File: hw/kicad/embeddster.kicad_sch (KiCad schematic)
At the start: 1 part, among them U1 ESP32-DEVKIT-V1

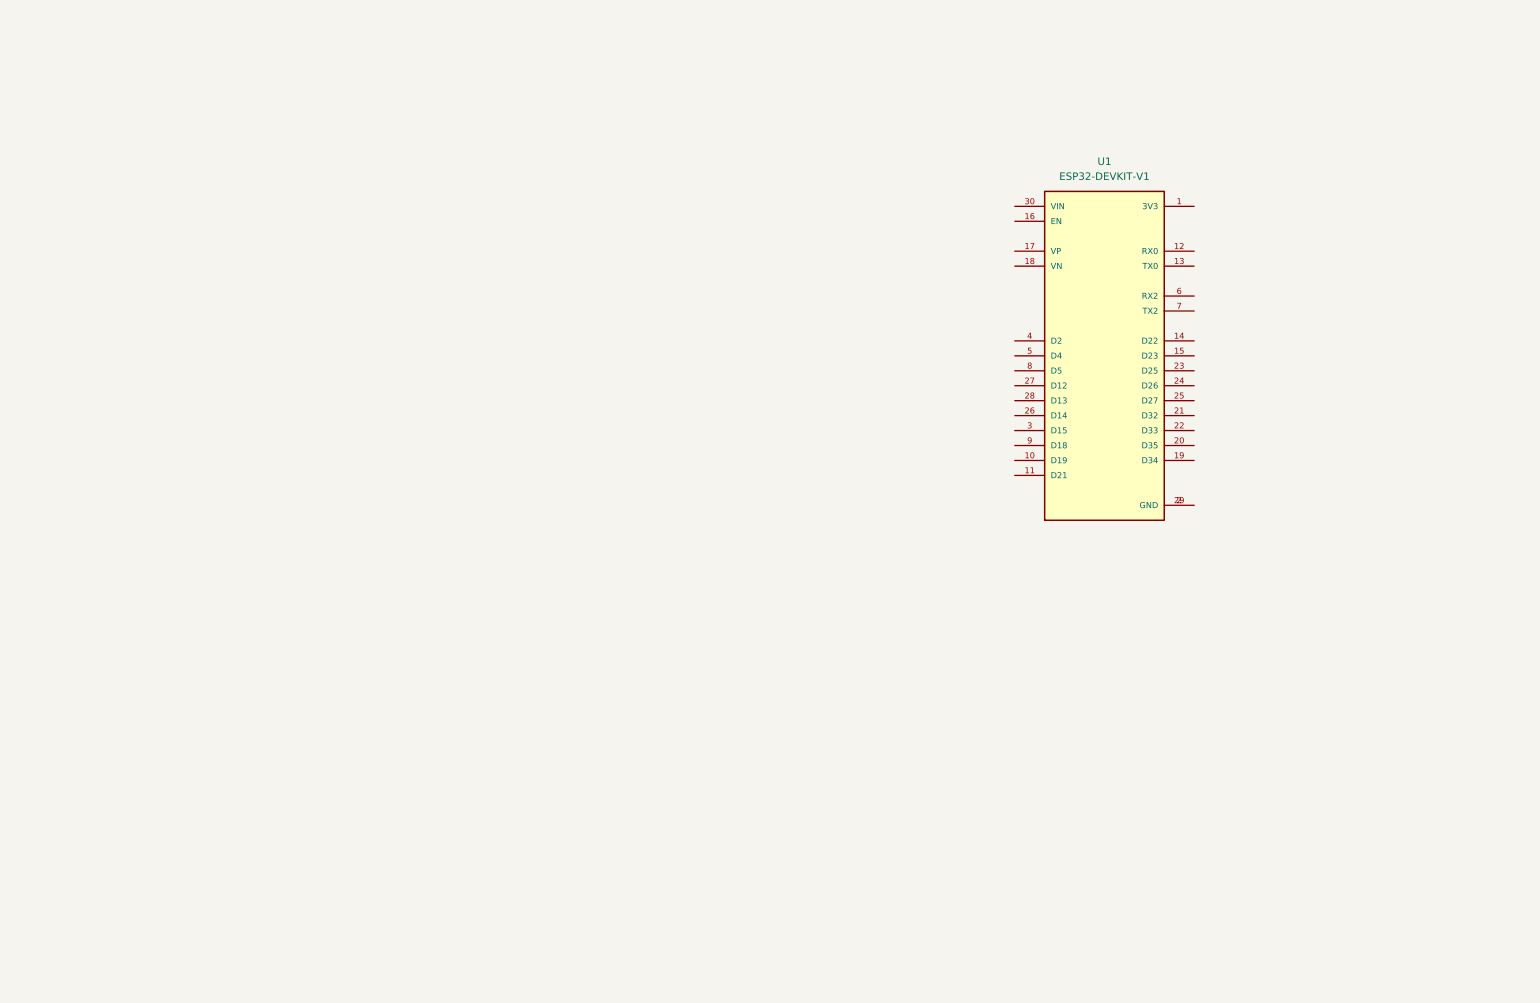
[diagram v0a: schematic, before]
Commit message: Pcb v0 (#1)
* Add custom KiCad symbol&footproint for PLACA_CAN_V20190517

* Add 3D models for PLACA_CAN_V20190517 connector pins

* Remove mounting holes from ESP32 footprint

* sch supporting tp1 & tp2

* Remove unnecessary zone definitions from ESP32 DevKit V1 footprint

* Add 3D models for ESP32 DevKit V1 connector pins

* pcb ready for fab

* Add pin assignment header for MCP, encoder, and 74HC595 control, based on PCB

* Add 4th quantum standoff to PCB, ground plane adjustments

* Add a WS2812B cell

* Add active low definition for encoder switch

* Update README to remove TP3 reference and clarify hardware interface

* Fix routing, remove old pic

* re-fix routing
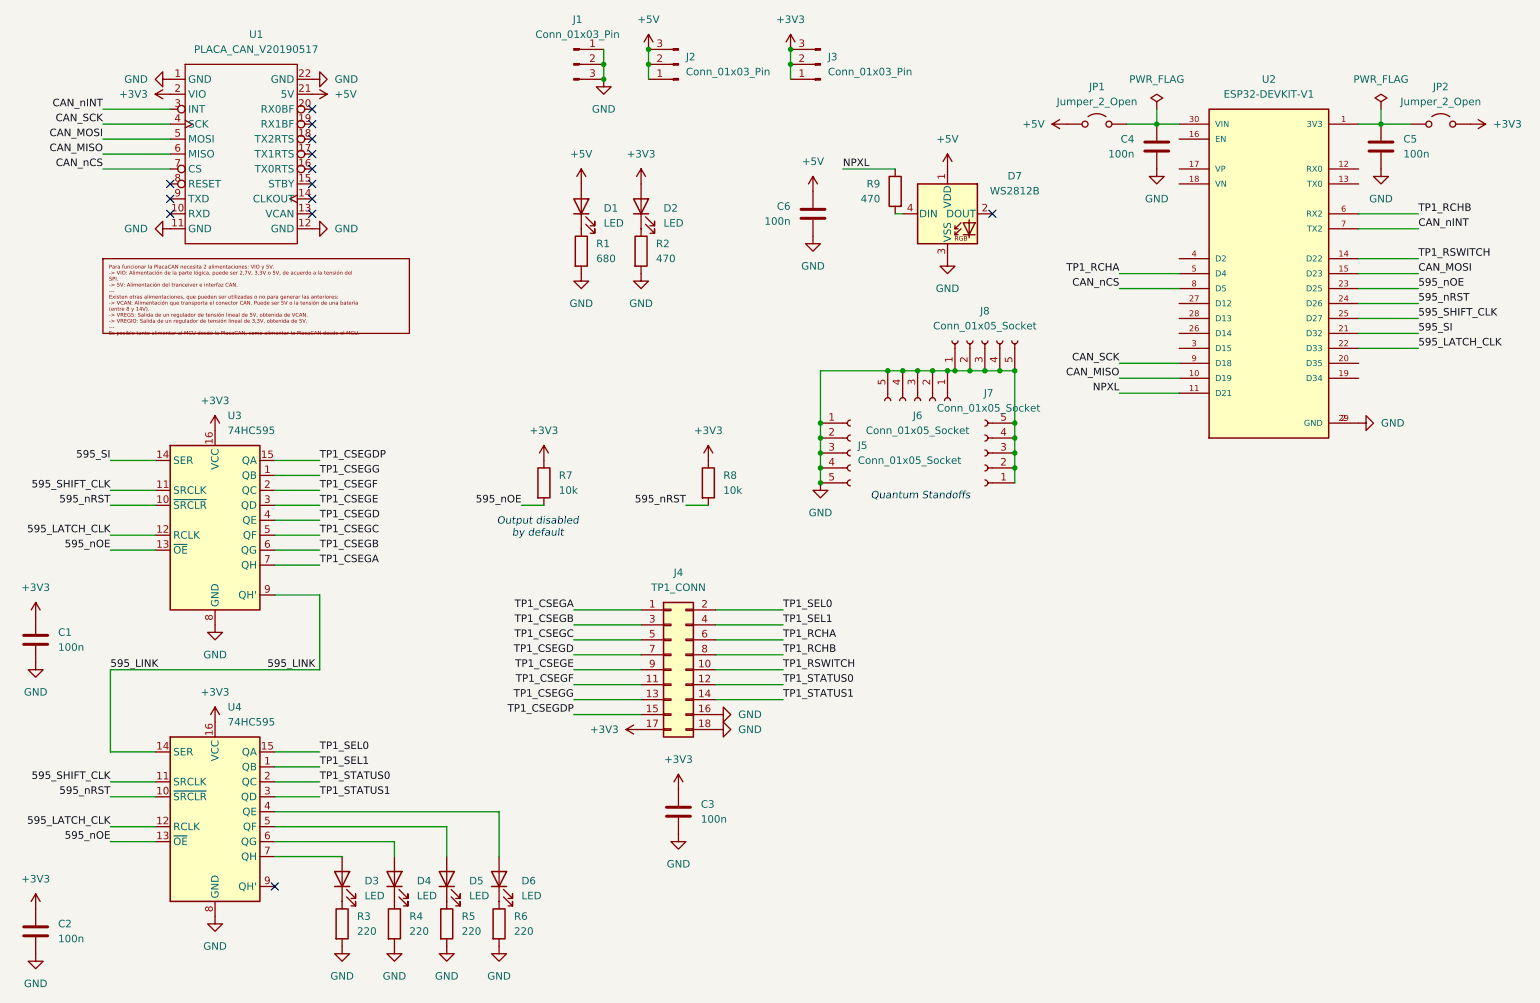
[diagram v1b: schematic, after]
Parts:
- added C1, C2, C3, C4, C5, C6: 100n, Capacitor_SMD:C_0805_2012Metric_Pad1.18x1.45mm_HandSolder, symbol Device:C
- added D1: LED, LED_THT:LED_D3.0mm, symbol Device:LED
- added D2, D3, D4, D5, D6: LED, LED_SMD:LED_0805_2012Metric_Pad1.15x1.40mm_HandSolder, symbol Device:LED
- added D7: WS2812B, LED_SMD:LED_WS2812B_PLCC4_5.0x5.0mm_P3.2mm, symbol LED:WS2812B
- added J1, J2, J3: Conn_01x03_Pin, Connector_PinHeader_2.54mm:PinHeader_1x03_P2.54mm_Vertical, symbol Connector:Conn_01x03_Pin
- added J4: TP1_CONN, Connector_PinSocket_2.54mm:PinSocket_2x09_P2.54mm_Vertical, symbol Connector_Generic:Conn_02x09_Odd_Even
- added J5, J6, J7, J8: Conn_01x05_Socket, Connector_PinSocket_2.54mm:PinSocket_1x05_P2.54mm_Vertical, symbol Connector:Conn_01x05_Socket
- added JP1, JP2: Jumper_2_Open, TestPoint:TestPoint_2Pads_Pitch2.54mm_Drill0.8mm, symbol Jumper:Jumper_2_Open
- added R1: 680, Resistor_SMD:R_0805_2012Metric_Pad1.20x1.40mm_HandSolder, symbol Device:R
- added R2, R9: 470, Resistor_SMD:R_0805_2012Metric_Pad1.20x1.40mm_HandSolder, symbol Device:R
- added R3, R4, R5, R6: 220, Resistor_SMD:R_0805_2012Metric_Pad1.20x1.40mm_HandSolder, symbol Device:R
- added R7, R8: 10k, Resistor_SMD:R_0805_2012Metric_Pad1.20x1.40mm_HandSolder, symbol Device:R
- added U1: PLACA_CAN_V20190517, PLACA_CAN_V20190517:PLACA_CAN_V20190517, symbol PLACA_CAN_V20190517:PLACA_CAN_V20190517
- added U3, U4: 74HC595, Package_SO:SOIC-16_3.9x9.9mm_P1.27mm, symbol 74xx:74HC595
- renumbered U1 to U2
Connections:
- net at U2.1 (3V3): now also C5.2, JP2.1 (A)
- net CAN_MISO: now reaches U2.10 (D19)
- net CAN_MISO: now also U1.6 (MISO)
- net NPXL: now reaches U2.11 (D21)
- net NPXL: now also R9.1
- net TP1_RSWITCH: now reaches U2.14 (D22)
- net TP1_RSWITCH: now also J4.10 (Pin_10)
- net CAN_MOSI: now reaches U2.15 (D23)
- net CAN_MOSI: now also U1.5 (MOSI)
- net GND: now reaches U2.2 (GND), U2.29 (GND)
- net GND: now also C1.1, C2.1, C3.1, C4.1, C5.1, C6.1, D7.3 (VSS), J1.1 (Pin_1), J1.2 (Pin_2), J1.3 (Pin_3), J4.16 (Pin_16), J4.18 (Pin_18), J5.1 (Pin_1), J5.2 (Pin_2), J5.3 (Pin_3), J5.4 (Pin_4), J5.5 (Pin_5), J6.1 (Pin_1), J6.2 (Pin_2), J6.3 (Pin_3), J6.4 (Pin_4), J6.5 (Pin_5), J7.1 (Pin_1), J7.2 (Pin_2), J7.3 (Pin_3), J7.4 (Pin_4), J7.5 (Pin_5), J8.1 (Pin_1), J8.2 (Pin_2), J8.3 (Pin_3), J8.4 (Pin_4), J8.5 (Pin_5), R1.2, R2.2, R3.2, R4.2, R5.2, R6.2, U1.1 (GND), U1.11 (GND), U1.12 (GND), U1.22 (GND), U3.8 (GND), U4.8 (GND)
- net 595_SI: now reaches U2.21 (D32)
- net 595_SI: now also U3.14 (SER)
- net 595_LATCH_CLK: now reaches U2.22 (D33)
- net 595_LATCH_CLK: now also U3.12 (RCLK), U4.12 (RCLK)
- net 595_nOE: now reaches U2.23 (D25)
- net 595_nOE: now also R7.2, U3.13 (~{OE}), U4.13 (~{OE})
- net 595_nRST: now reaches U2.24 (D26)
- net 595_nRST: now also R8.2, U3.10 (~{SRCLR}), U4.10 (~{SRCLR})
- net 595_SHIFT_CLK: now reaches U2.25 (D27)
- net 595_SHIFT_CLK: now also U3.11 (SRCLK), U4.11 (SRCLK)
- net at U2.30 (VIN): now also C4.2, JP1.2 (B)
- net TP1_RCHA: now reaches U2.5 (D4)
- net TP1_RCHA: now also J4.6 (Pin_6)
- net TP1_RCHB: now reaches U2.6 (RX2)
- net TP1_RCHB: now also J4.8 (Pin_8)
- net CAN_nINT: now reaches U2.7 (TX2)
- net CAN_nINT: now also U1.3 (INT)
- net CAN_nCS: now reaches U2.8 (D5)
- net CAN_nCS: now also U1.7 (CS)
- net CAN_SCK: now reaches U2.9 (D18)
- net CAN_SCK: now also U1.4 (SCK)
- new net: D6.2 (A), U4.4 (QE)
- new net: D5.2 (A), U4.5 (QF)
- new net: D4.2 (A), U4.6 (QG)
- new net: D3.2 (A), U4.7 (QH)
- new net: D1.1 (K), R1.1
- new net: D2.1 (K), R2.1
- new net: D6.1 (K), R6.1
- new net: D3.1 (K), R3.1
- new net: D4.1 (K), R4.1
- new net: D5.1 (K), R5.1
- new net: D7.4 (DIN), R9.2
- new net +3V3: C1.2, C2.2, C3.2, D2.2 (A), J3.1 (Pin_1), J3.2 (Pin_2), J3.3 (Pin_3), J4.17 (Pin_17), JP2.2 (B), R7.1, R8.1, U1.2 (VIO), U3.16 (VCC), U4.16 (VCC)
- new net +5V: C6.2, D1.2 (A), D7.1 (VDD), J2.1 (Pin_1), J2.2 (Pin_2), J2.3 (Pin_3), JP1.1 (A), U1.21 (5V)
- new net 595_LINK: U3.9 (QH'), U4.14 (SER)
- new net TP1_CSEGA: J4.1 (Pin_1), U3.7 (QH)
- new net TP1_CSEGB: J4.3 (Pin_3), U3.6 (QG)
- new net TP1_CSEGC: J4.5 (Pin_5), U3.5 (QF)
- new net TP1_CSEGD: J4.7 (Pin_7), U3.4 (QE)
- new net TP1_CSEGDP: J4.15 (Pin_15), U3.15 (QA)
- new net TP1_CSEGE: J4.9 (Pin_9), U3.3 (QD)
- new net TP1_CSEGF: J4.11 (Pin_11), U3.2 (QC)
- new net TP1_CSEGG: J4.13 (Pin_13), U3.1 (QB)
- new net TP1_SEL0: J4.2 (Pin_2), U4.15 (QA)
- new net TP1_SEL1: J4.4 (Pin_4), U4.1 (QB)
- new net TP1_STATUS0: J4.12 (Pin_12), U4.2 (QC)
- new net TP1_STATUS1: J4.14 (Pin_14), U4.3 (QD)
- no-connect marks 0 -> 13
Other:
- note added: "Output disabled by default"
- note added: "Quantum Standoffs"
- title: (none) -> Embeddster PCB
- moved on the sheet: U2
